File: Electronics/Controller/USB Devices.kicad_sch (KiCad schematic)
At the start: 20 parts, among them U10 FT232RL, U11 FT232RL, U8 FT232RL, U9 FT232RL

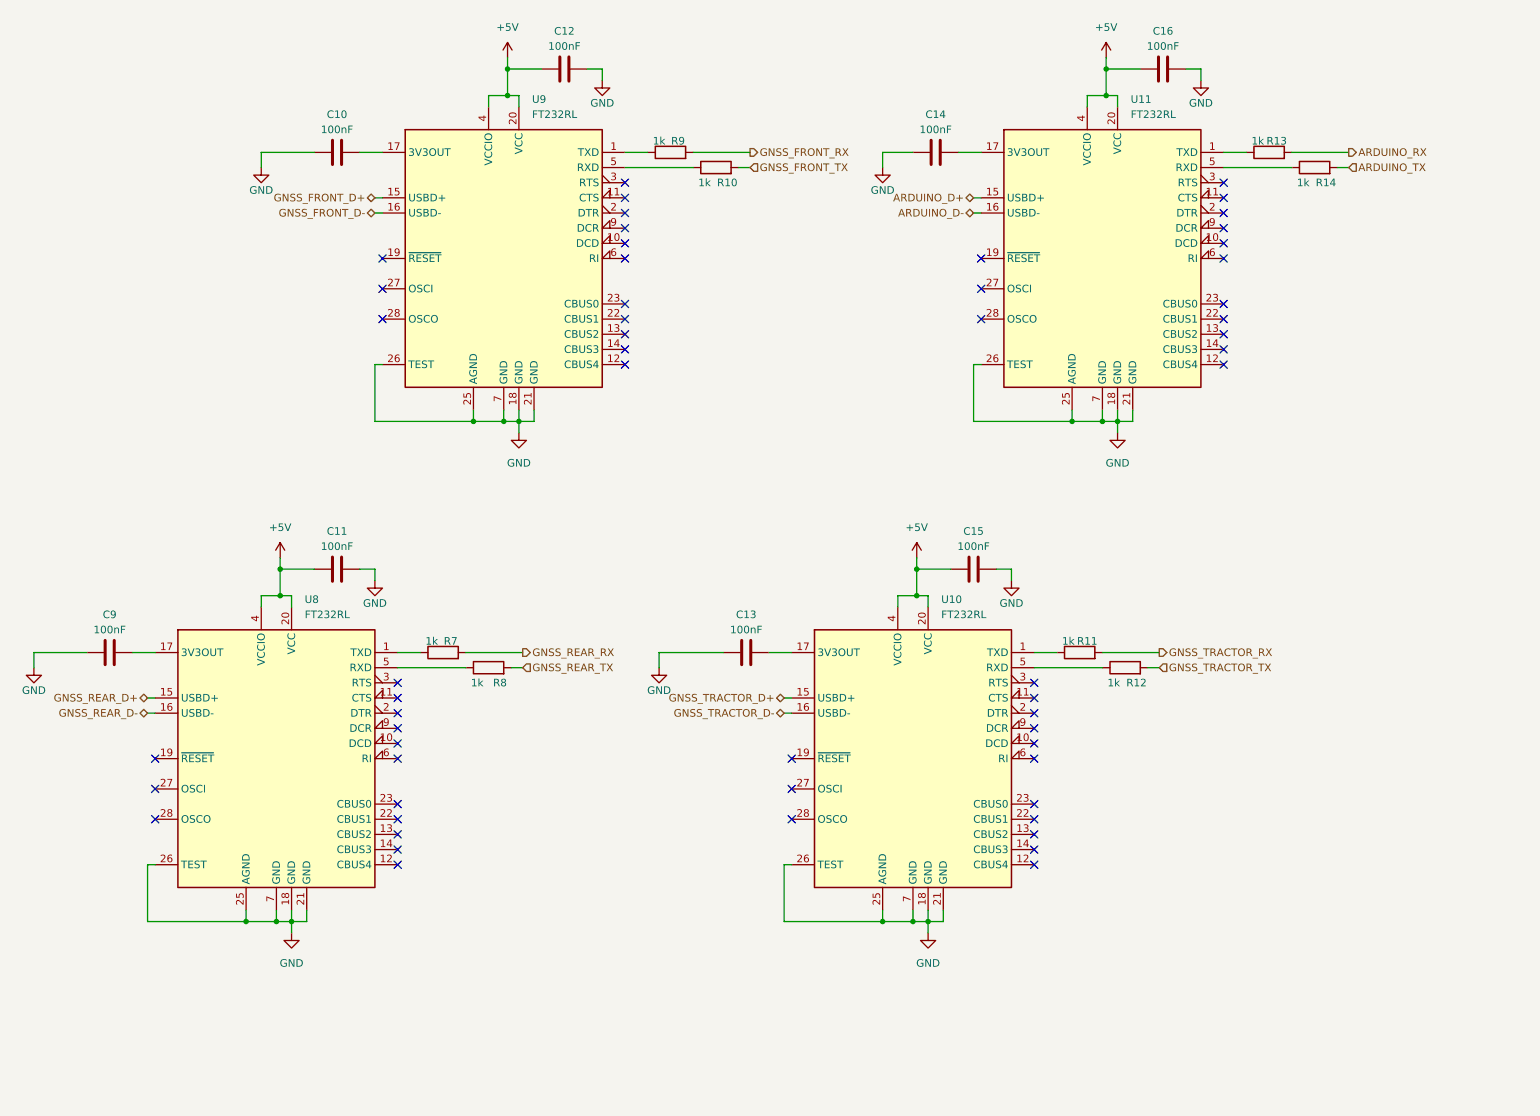
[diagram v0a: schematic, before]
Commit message: Working on schematic. Added datasheets.
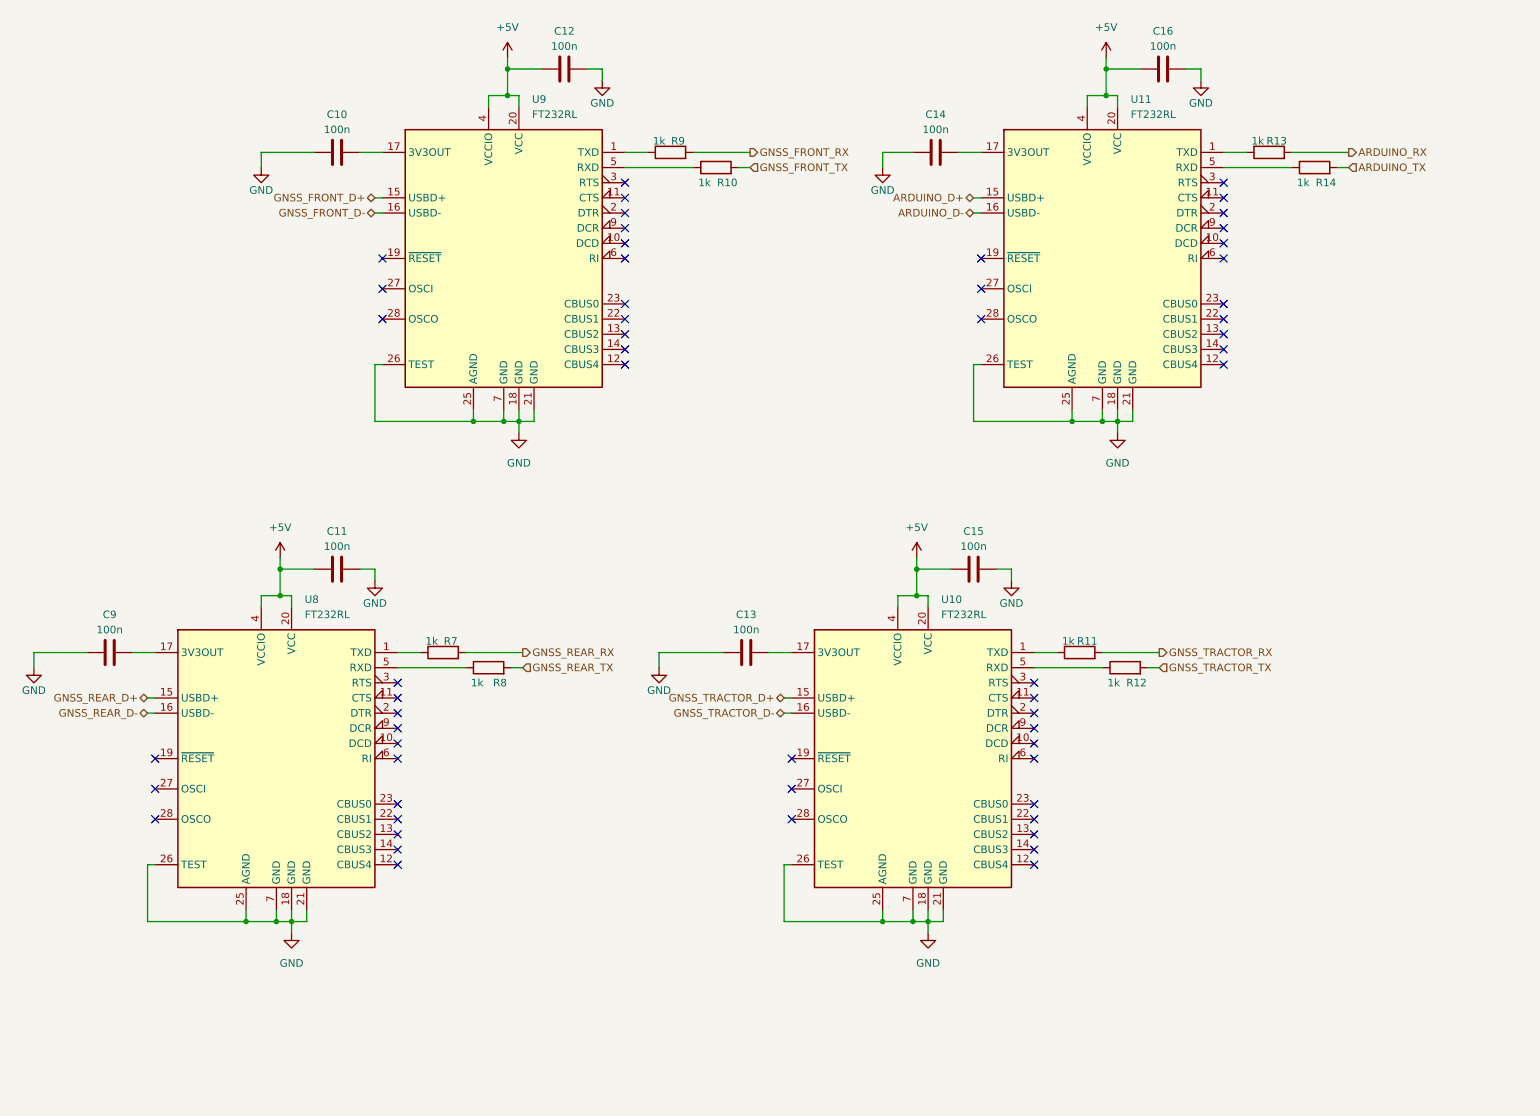
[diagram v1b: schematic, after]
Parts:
- C10, C11, C12, C13, C14, C15, C16, C9: value 100nF -> 100n
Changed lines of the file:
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@@
   (title_block
     (title "Tandem Leveller Controller")
-    (date "2025-02-13")
+    (date "2025-02-14")
     (rev "V1.0")
     (company "(C) andy@britishideas.com 2025")
@@
       (effects (font (size 1.27 1.27)))
     )
-    (property "Value" "100nF" (at 107.315 19.685 90)
+    (property "Value" "100n" (at 107.315 19.685 90)
       (effects (font (size 1.27 1.27)))
     )
@@
       (effects (font (size 1.27 1.27)))
     )
-    (property "Value" "100nF" (at 137.795 117.475 90)
+    (property "Value" "100n" (at 137.795 117.475 90)
       (effects (font (size 1.27 1.27)))
     )
@@
       (effects (font (size 1.27 1.27)))
     )
-    (property "Value" "100nF" (at 175.895 103.505 90)
+    (property "Value" "100n" (at 175.895 103.505 90)
       (effects (font (size 1.27 1.27)))
     )
@@
       (effects (font (size 1.27 1.27)))
     )
-    (property "Value" "100nF" (at 169.545 33.655 90)
+    (property "Value" "100n" (at 169.545 33.655 90)
       (effects (font (size 1.27 1.27)))
     )
@@
       (effects (font (size 1.27 1.27)))
     )
-    (property "Value" "100nF" (at 69.215 33.655 90)
+    (property "Value" "100n" (at 69.215 33.655 90)
       (effects (font (size 1.27 1.27)))
     )
@@
       (effects (font (size 1.27 1.27)))
     )
-    (property "Value" "100nF" (at 69.215 103.505 90)
+    (property "Value" "100n" (at 69.215 103.505 90)
       (effects (font (size 1.27 1.27)))
     )
@@
       (effects (font (size 1.27 1.27)))
     )
-    (property "Value" "100nF" (at 207.645 19.685 90)
+    (property "Value" "100n" (at 207.645 19.685 90)
       (effects (font (size 1.27 1.27)))
     )
@@
       (effects (font (size 1.27 1.27)))
     )
-    (property "Value" "100nF" (at 31.115 117.475 90)
-      (effects (font (size 1.27 1.27)))
-    )
+    (property "Value" "100n" (at 31.115 117.475 90)
+      (effects (font (size 1.27 1.27)))
+    )

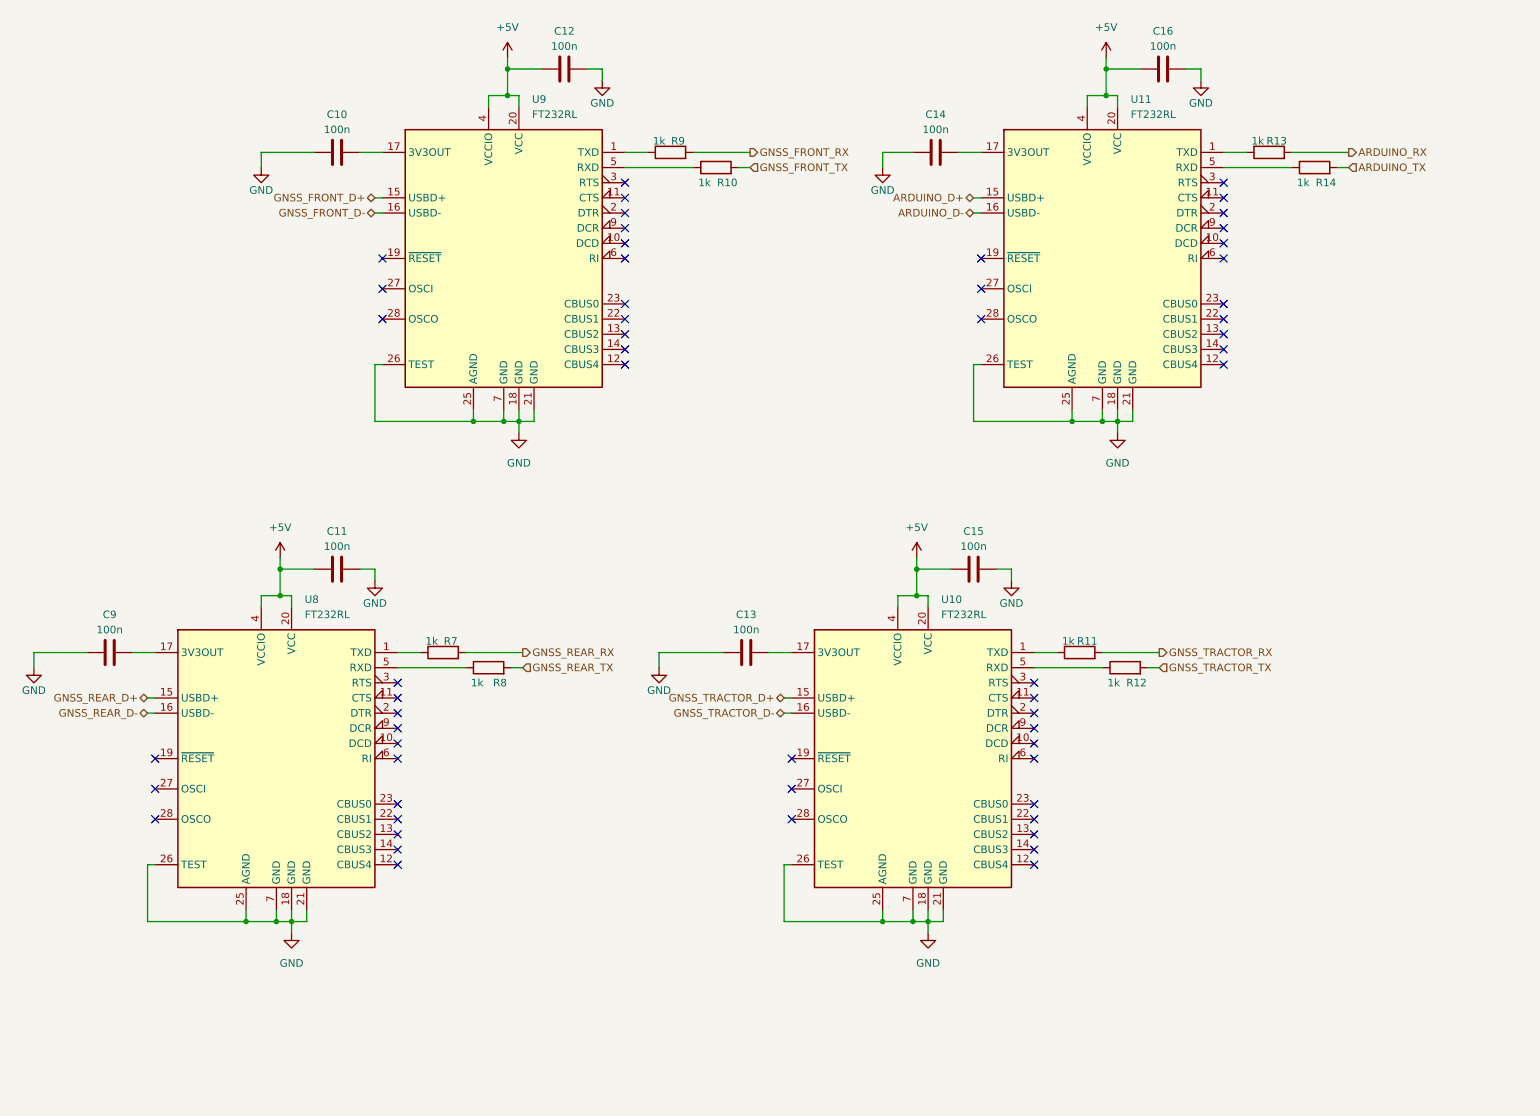
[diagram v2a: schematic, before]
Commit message: Updated schematic. Added footprints for all components.
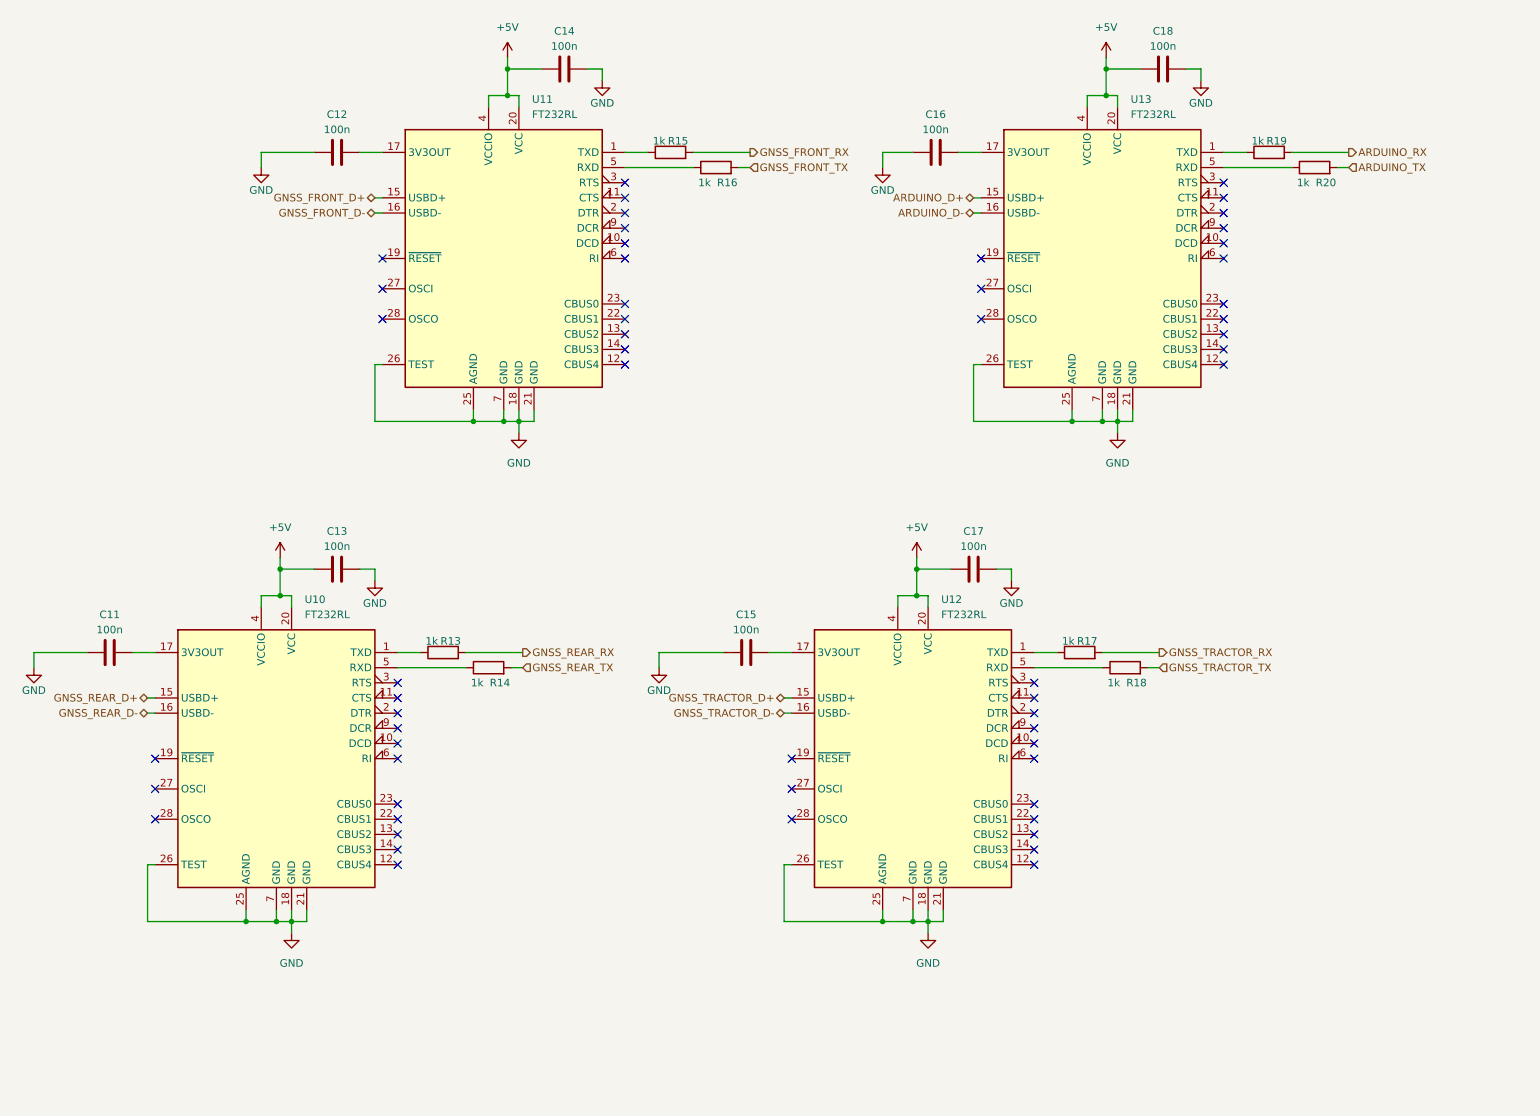
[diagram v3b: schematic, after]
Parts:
- C11: renamed from C9; footprint (none) -> Capacitor_SMD:C_0805_2012Metric
- C12: renamed from C10; footprint (none) -> Capacitor_SMD:C_0805_2012Metric
- C13: renamed from C11; footprint (none) -> Capacitor_SMD:C_0805_2012Metric
- C14: renamed from C12; footprint (none) -> Capacitor_SMD:C_0805_2012Metric
- C15: renamed from C13; footprint (none) -> Capacitor_SMD:C_0805_2012Metric
- C16: renamed from C14; footprint (none) -> Capacitor_SMD:C_0805_2012Metric
- C17: renamed from C15; footprint (none) -> Capacitor_SMD:C_0805_2012Metric
- C18: renamed from C16; footprint (none) -> Capacitor_SMD:C_0805_2012Metric
- R13: renamed from R7; footprint (none) -> Resistor_SMD:R_0805_2012Metric
- R14: renamed from R8; footprint (none) -> Resistor_SMD:R_0805_2012Metric
- R15: renamed from R9; footprint (none) -> Resistor_SMD:R_0805_2012Metric
- R16: renamed from R10; footprint (none) -> Resistor_SMD:R_0805_2012Metric
- R17: renamed from R11; footprint (none) -> Resistor_SMD:R_0805_2012Metric
- R18: renamed from R12; footprint (none) -> Resistor_SMD:R_0805_2012Metric
- R19: renamed from R13; footprint (none) -> Resistor_SMD:R_0805_2012Metric
- R20: renamed from R14; footprint (none) -> Resistor_SMD:R_0805_2012Metric
- renumbered U8 to U10, U9 to U11, U10 to U12, U11 to U13

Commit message: Changed switches and lamps. Removed status LEDs. Working on PCB layout.
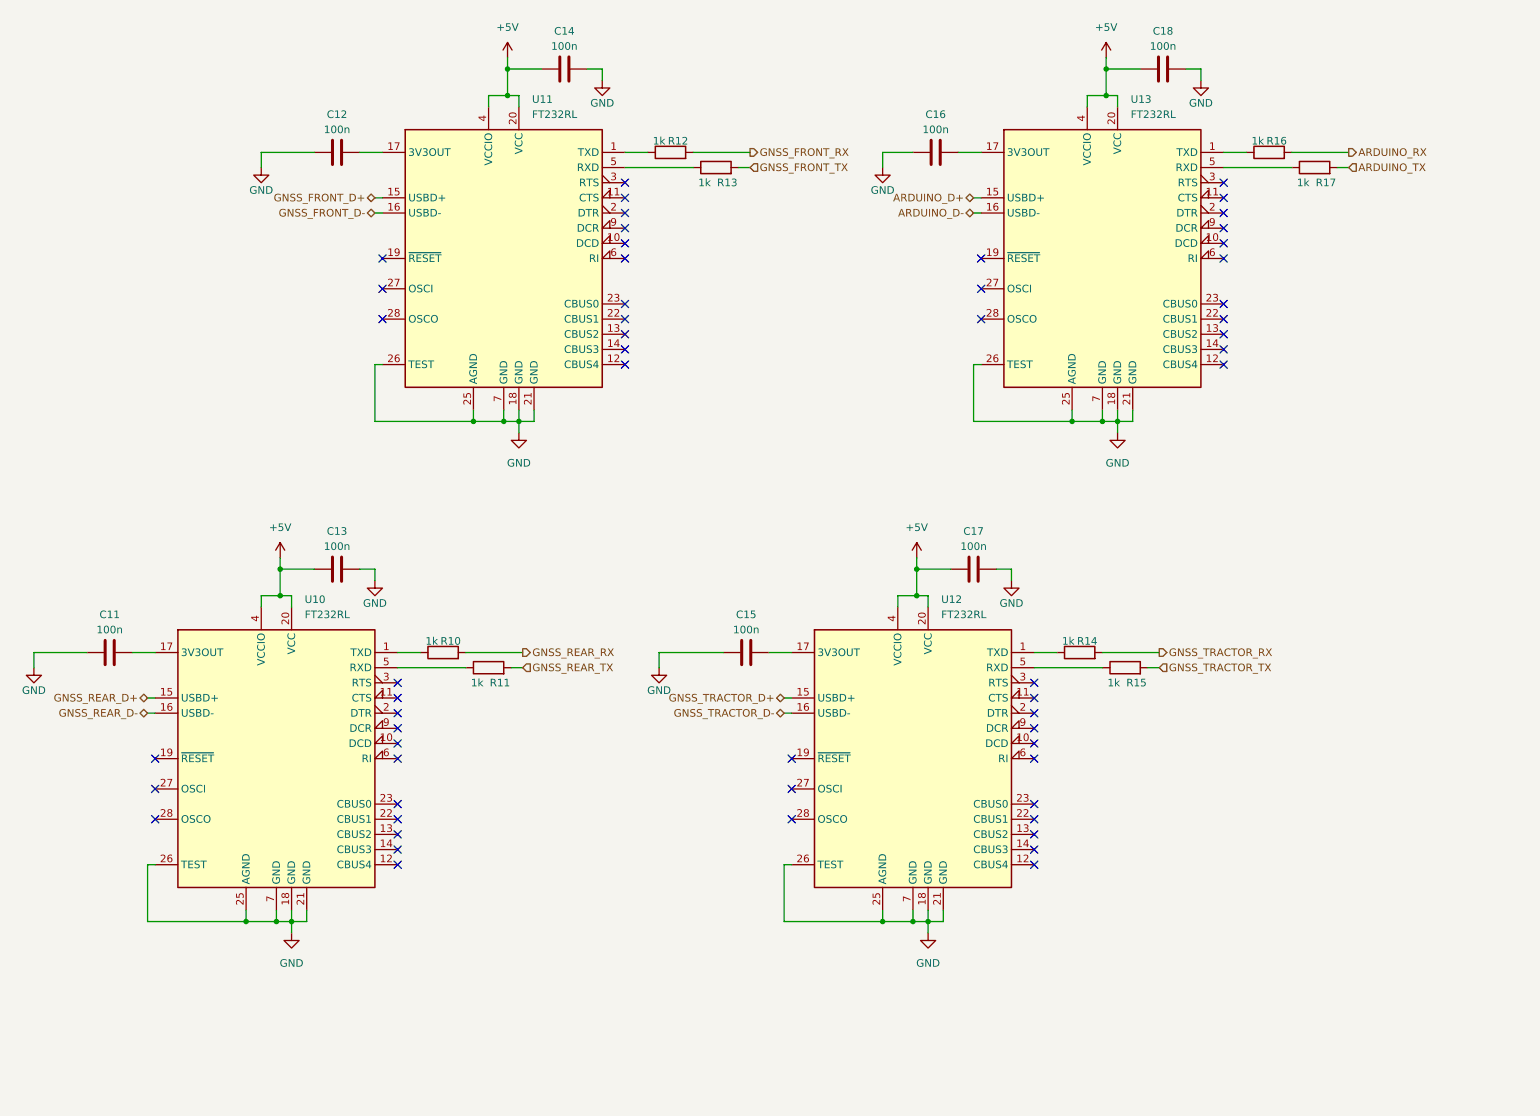
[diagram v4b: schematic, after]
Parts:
- renumbered R13 to R10, R14 to R11, R15 to R12, R16 to R13, R17 to R14, R18 to R15, R19 to R16, R20 to R17
